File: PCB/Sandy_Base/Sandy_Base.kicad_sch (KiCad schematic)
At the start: 165 parts, among them J1 Conn_02x02_Top_Bottom, J10 TP3, J2 Conn_02x02_Top_Bottom, J3 Conn_02x02_Top_Bottom, J4 Conn_02x02_Top_Bottom, J5 Conn_02x02_Top_Bottom, J6 Conn_02x02_Top_Bottom, J7 USB_C_Receptacle_USB2.0, J8 TP1, J9 TP2, SW1 BOOT, SW2 RESET, U1 NCP1117-3.3_SOT223, U2 RP2040, U3 W25Q128JVPIQ, Y1 12MHz

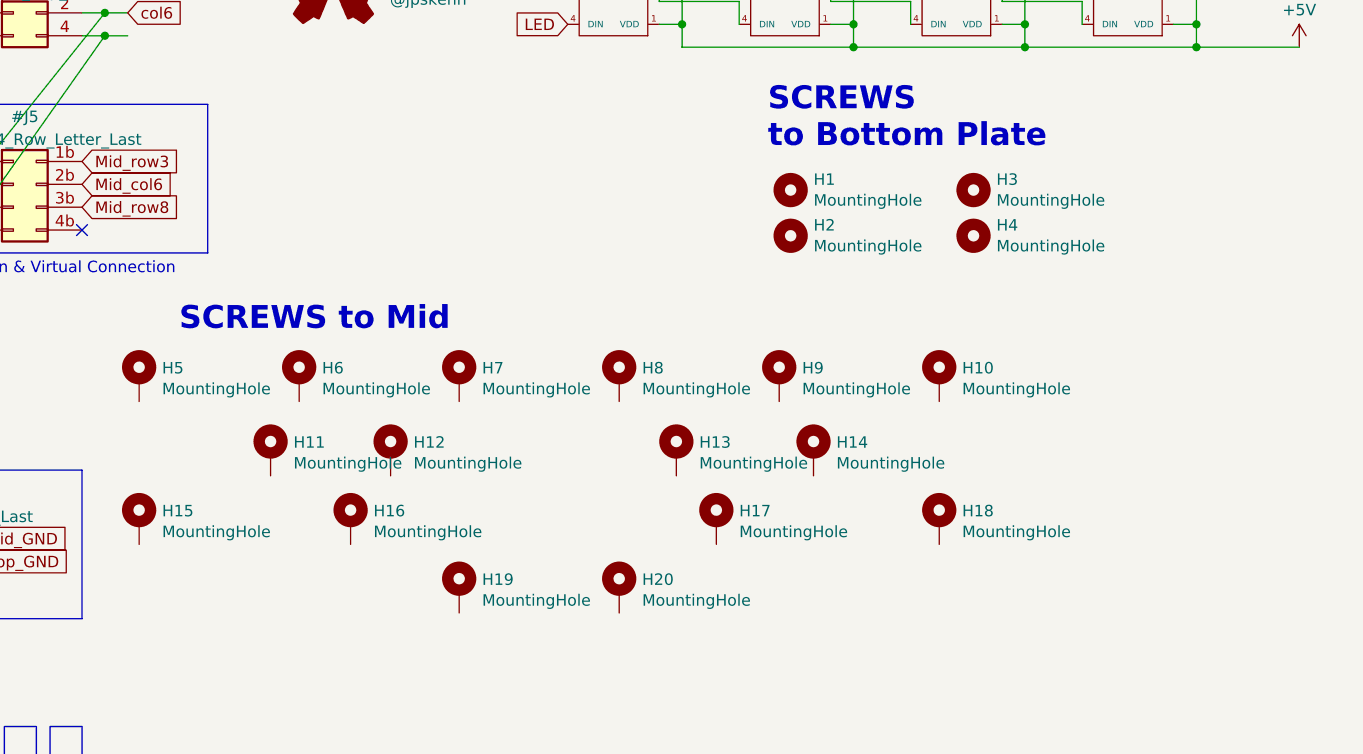
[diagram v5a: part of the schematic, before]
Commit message: ネジ穴調整、追加
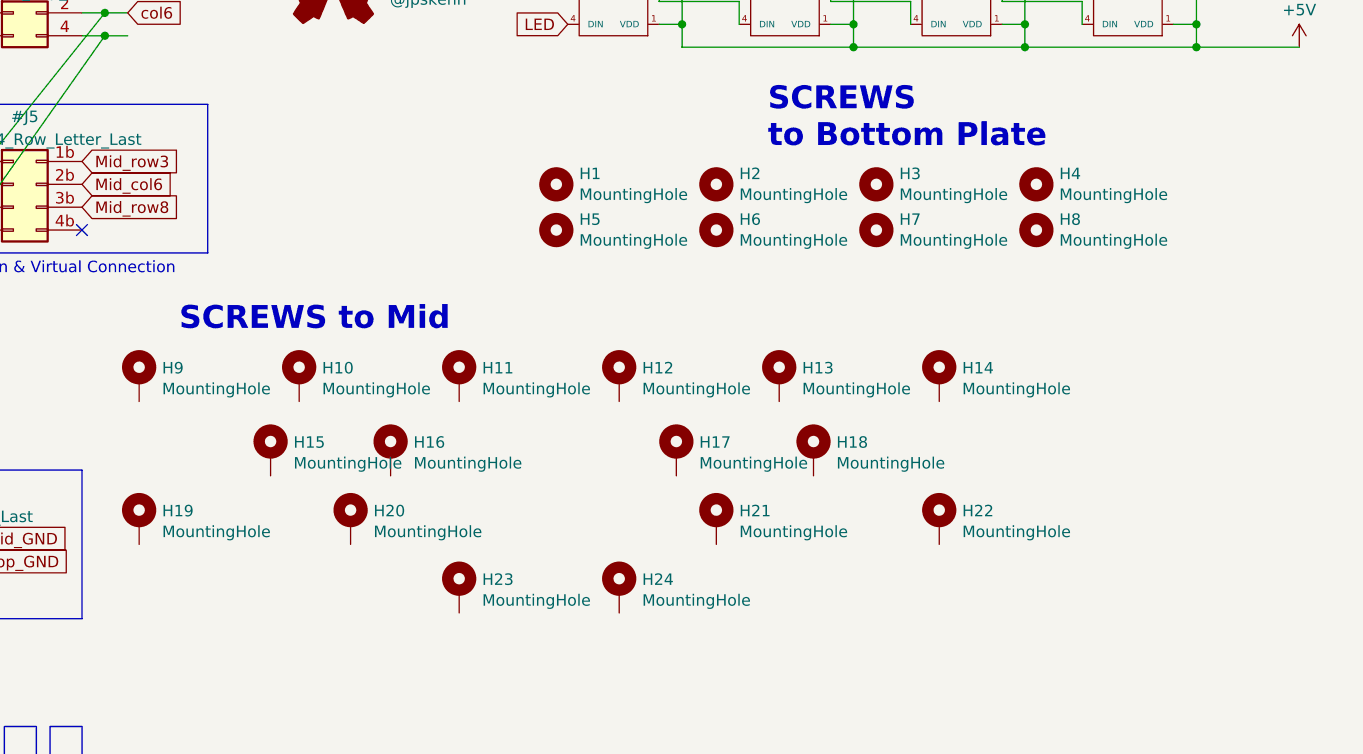
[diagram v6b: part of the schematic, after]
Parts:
- added H5, H6, H7, H8: MountingHole, locallib:MountingHole_2.2mm_M2_No_Cu, symbol Mechanical:MountingHole
- renumbered H6 to H10, H7 to H11, H8 to H12, H9 to H13, H10 to H14, H11 to H15, H12 to H16, H13 to H17, H14 to H18, H15 to H19, H16 to H20, H17 to H21, H18 to H22, H19 to H23, H20 to H24, H5 to H9
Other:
- moved on the sheet: H1, H2, H3, H4

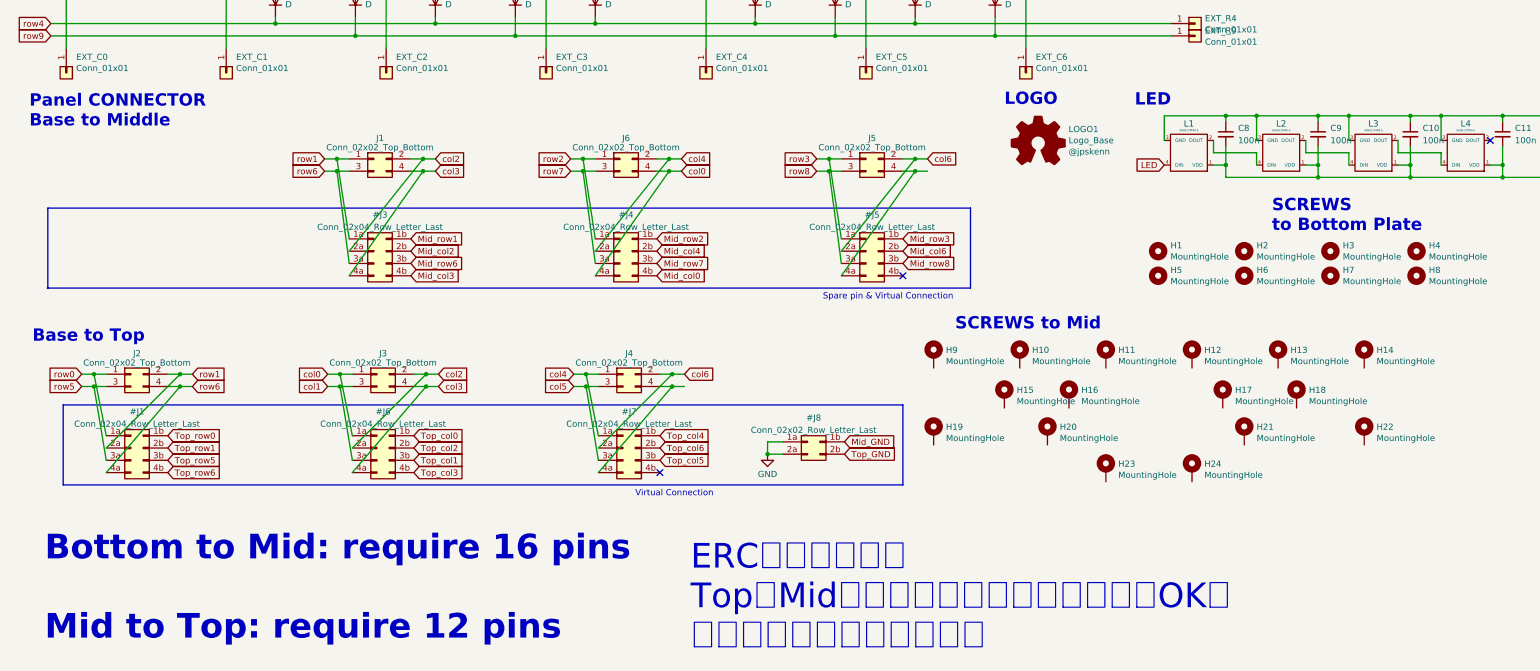
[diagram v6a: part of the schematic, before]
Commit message: ネジ穴と接続するピンを調整中
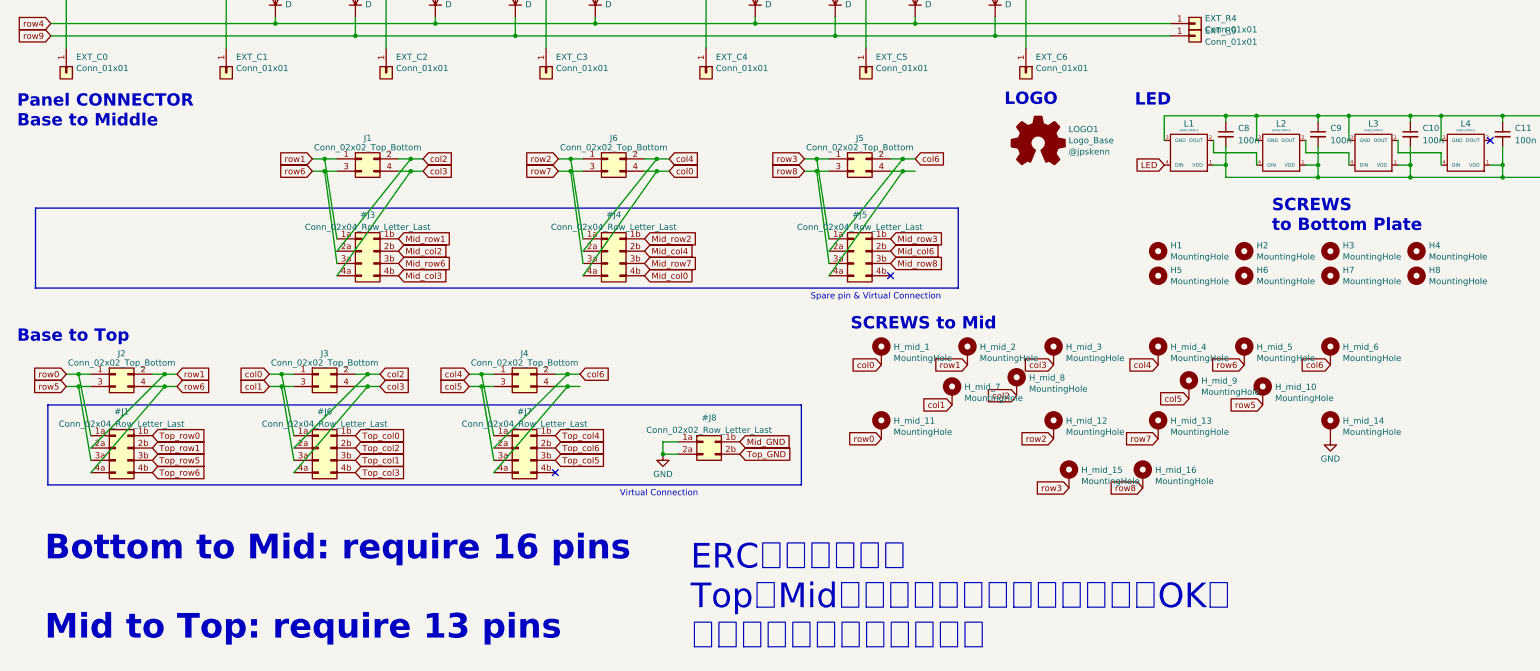
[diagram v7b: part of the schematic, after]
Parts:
- renumbered H9 to H_mid_1, H18 to H_mid_10, H19 to H_mid_11, H20 to H_mid_12, H21 to H_mid_13, H22 to H_mid_14, H23 to H_mid_15, H24 to H_mid_16, H10 to H_mid_2, H11 to H_mid_3, H12 to H_mid_4, H13 to H_mid_5, H14 to H_mid_6, H15 to H_mid_7, H16 to H_mid_8, H17 to H_mid_9
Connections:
- net GND: now also H_mid_14.1
- net col0: now also H_mid_1.1
- net col1: now also H_mid_7.1
- net col2: now also H_mid_8.1
- net col3: now also H_mid_3.1
- net col4: now also H_mid_4.1
- net col5: now also H_mid_9.1
- net col6: now also H_mid_6.1
- net row0: now also H_mid_11.1
- net row1: now also H_mid_2.1
- net row2: now also H_mid_12.1
- net row3: now also H_mid_15.1
- net row5: now also H_mid_10.1
- net row6: now also H_mid_5.1
- net row7: now also H_mid_13.1
- net row8: now also H_mid_16.1
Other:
- note added: "Bottom to Mid: require 16 pins Mid to Top: require 13 pins"
- note removed: "Bottom to Mid: require 16 pins Mid to Top: require 12 pins"
- moved on the sheet: H_mid_1, H_mid_10, H_mid_11, H_mid_12, H_mid_13, H_mid_14, H_mid_15, H_mid_16, H_mid_2, H_mid_3, H_mid_4, H_mid_5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

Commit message: JST SH コネクタのフットプリントにコートヤードを追加
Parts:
- J1, J2, J3, J4, J5, J6: footprint locallib:JST_SH_SM04B-SRSS-TB_1x04-1MP_P1.00mm_Horizontal_wCable_housing_spare_pin -> locallib:JST_SH_SM04B-SRSS-TB_1x04-1MP_P1.00mm_Horizontal_wCable_housing_spare_pin_courtyard
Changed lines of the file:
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@@
 			)
 		)
-		(property "Footprint" "locallib:JST_SH_SM04B-SRSS-TB_1x04-1MP_P1.00mm_Horizontal_wCable_housing_spare_pin"
+		(property "Footprint" "locallib:JST_SH_SM04B-SRSS-TB_1x04-1MP_P1.00mm_Horizontal_wCable_housing_spare_pin_courtyard"
 			(at 134.62 214.63 0)
 			(effects
@@
 			)
 		)
-		(property "Footprint" "locallib:JST_SH_SM04B-SRSS-TB_1x04-1MP_P1.00mm_Horizontal_wCable_housing_spare_pin"
+		(property "Footprint" "locallib:JST_SH_SM04B-SRSS-TB_1x04-1MP_P1.00mm_Horizontal_wCable_housing_spare_pin_courtyard"
 			(at 185.42 214.63 0)
 			(effects
@@
 			)
 		)
-		(property "Footprint" "locallib:JST_SH_SM04B-SRSS-TB_1x04-1MP_P1.00mm_Horizontal_wCable_housing_spare_pin"
+		(property "Footprint" "locallib:JST_SH_SM04B-SRSS-TB_1x04-1MP_P1.00mm_Horizontal_wCable_housing_spare_pin_courtyard"
 			(at 116.205 259.08 0)
 			(effects
@@
 			)
 		)
-		(property "Footprint" "locallib:JST_SH_SM04B-SRSS-TB_1x04-1MP_P1.00mm_Horizontal_wCable_housing_spare_pin"
+		(property "Footprint" "locallib:JST_SH_SM04B-SRSS-TB_1x04-1MP_P1.00mm_Horizontal_wCable_housing_spare_pin_courtyard"
 			(at 74.93 259.08 0)
 			(effects
@@
 			)
 		)
-		(property "Footprint" "locallib:JST_SH_SM04B-SRSS-TB_1x04-1MP_P1.00mm_Horizontal_wCable_housing_spare_pin"
+		(property "Footprint" "locallib:JST_SH_SM04B-SRSS-TB_1x04-1MP_P1.00mm_Horizontal_wCable_housing_spare_pin_courtyard"
 			(at 83.82 214.63 0)
 			(effects
@@
 			)
 		)
-		(property "Footprint" "locallib:JST_SH_SM04B-SRSS-TB_1x04-1MP_P1.00mm_Horizontal_wCable_housing_spare_pin"
+		(property "Footprint" "locallib:JST_SH_SM04B-SRSS-TB_1x04-1MP_P1.00mm_Horizontal_wCable_housing_spare_pin_courtyard"
 			(at 33.02 259.08 0)
 			(effects
